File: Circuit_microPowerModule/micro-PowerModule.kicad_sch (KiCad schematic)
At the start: 7 parts, among them J2 Jack-DC, J3 Screw_Terminal_01x02

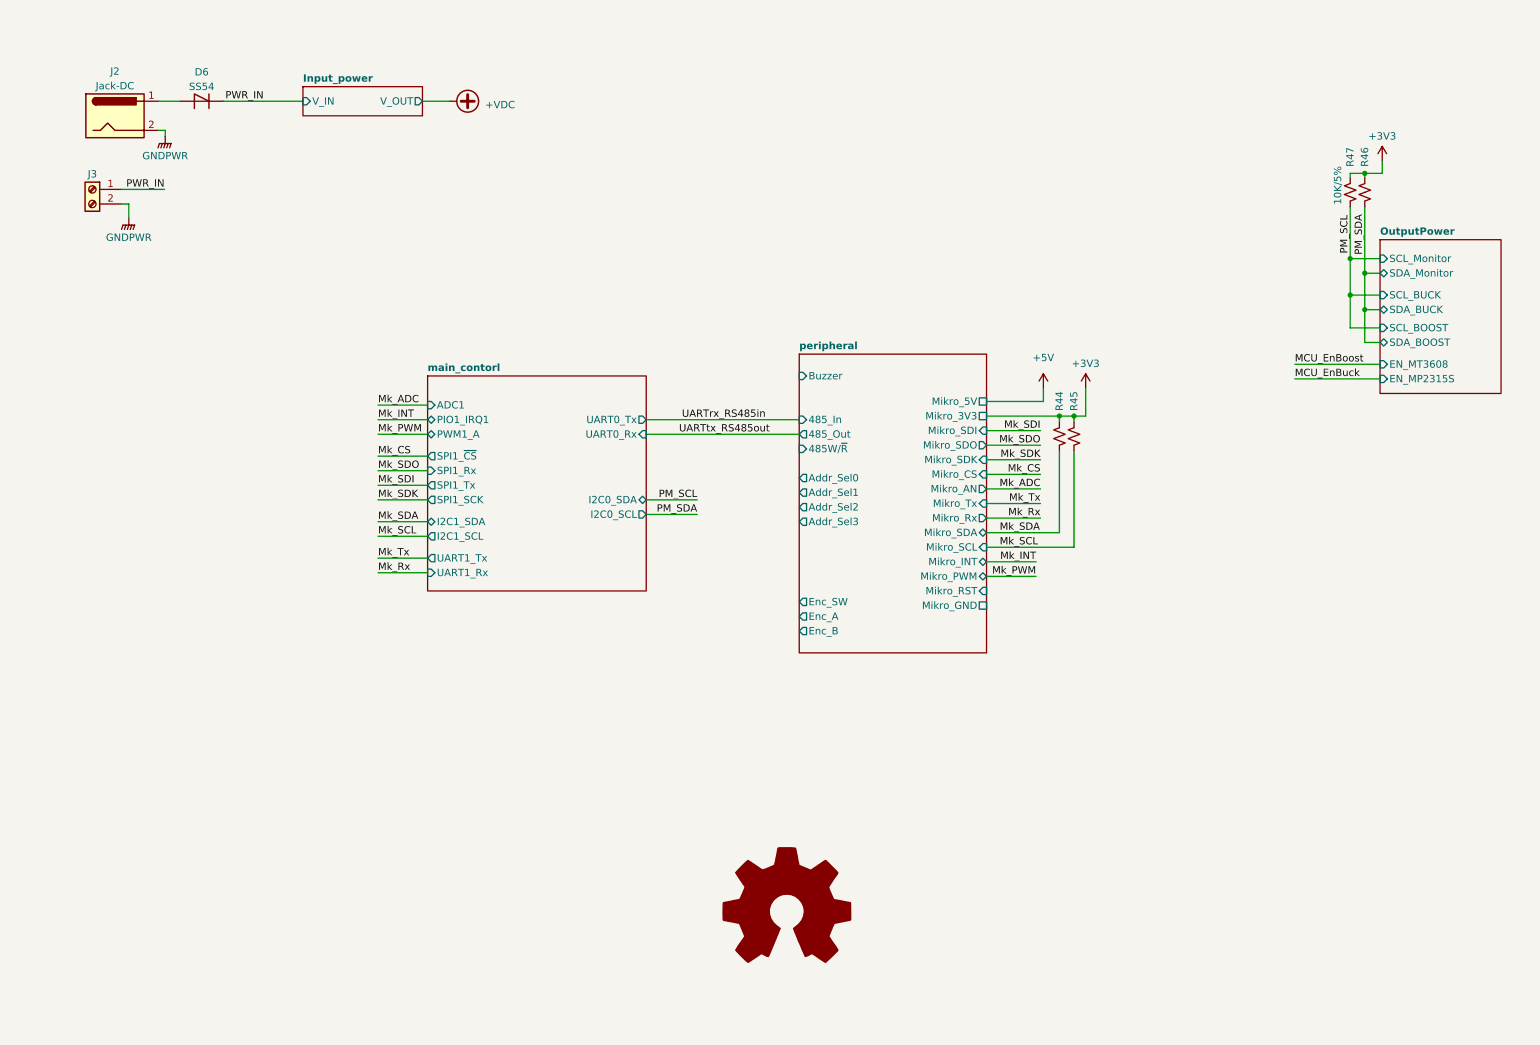
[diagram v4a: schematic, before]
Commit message: Completed microcontroller unit pin planning
update schematic
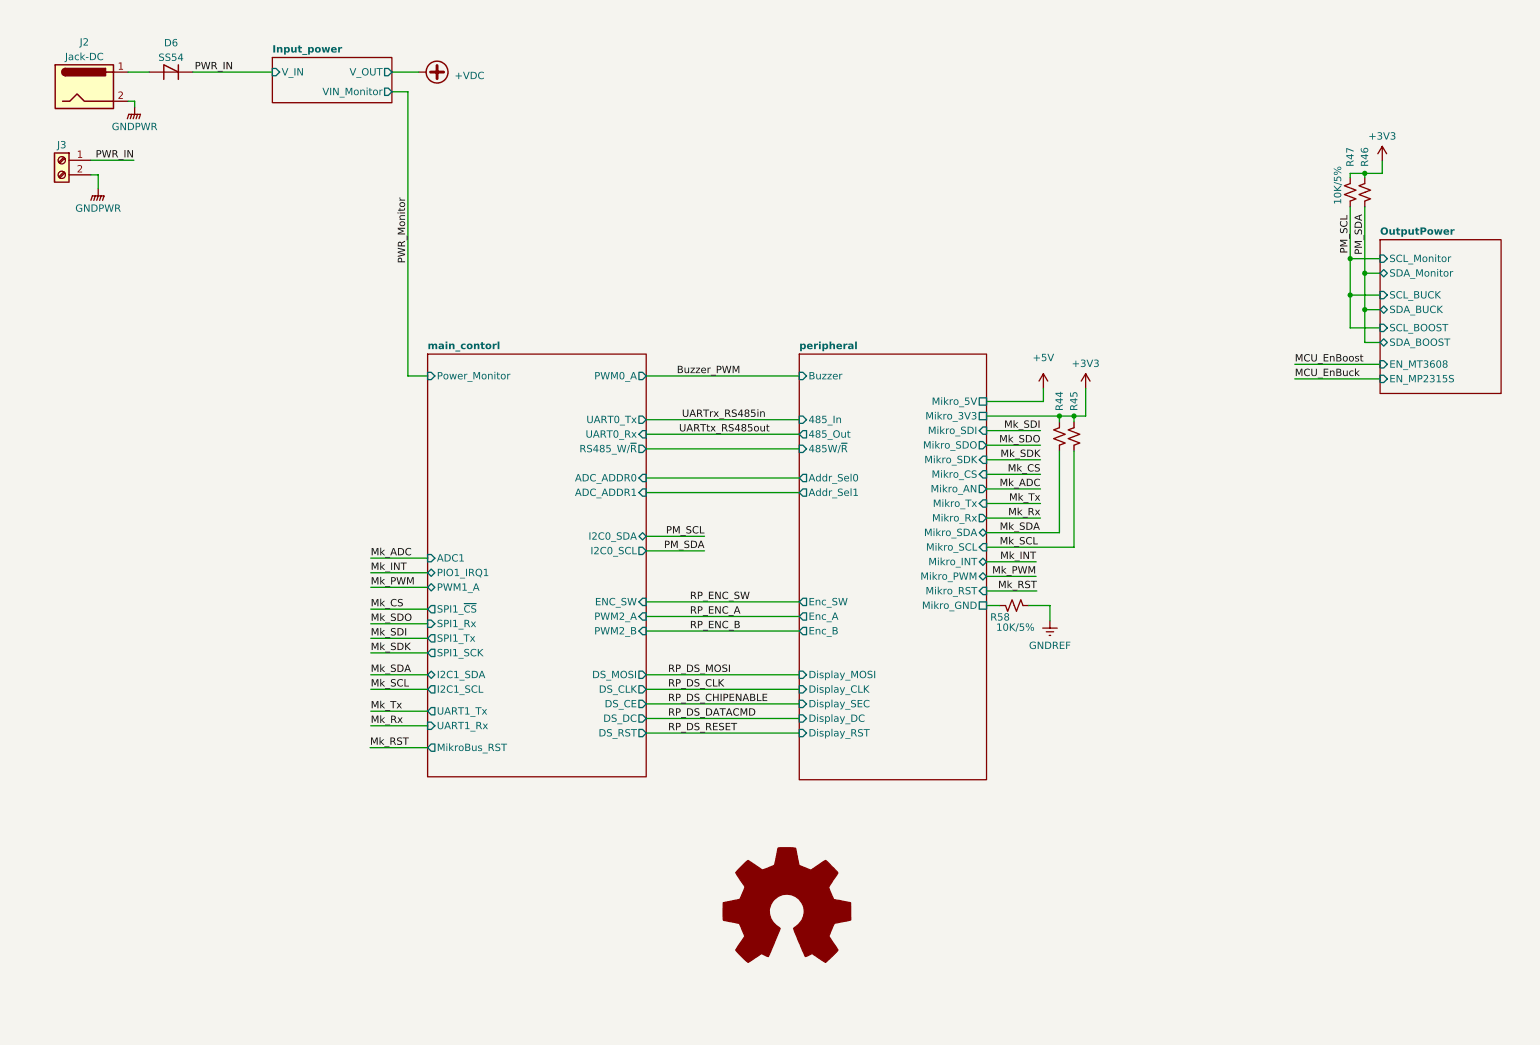
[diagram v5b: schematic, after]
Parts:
- added R58: 10K/5%, Resistor_SMD:R_0603_1608Metric, symbol Device:R_Small_US
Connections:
- net peripheral/Mikro_GND: now also R58.2
- new net GNDREF: R58.1
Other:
- sheet Input_power ports: added VIN_Monitor; removed none
- sheet main_contorl ports: added ADC_ADDR0, ADC_ADDR1, DS_CE, DS_CLK, DS_DC, DS_MOSI, DS_RST, ENC_SW, MikroBus_RST, PWM0_A, PWM2_A, PWM2_B, Power_Monitor, RS485_W/~{R}; removed none
- sheet peripheral ports: added Display_CLK, Display_DC, Display_MOSI, Display_RST, Display_SEC; removed Addr_Sel2, Addr_Sel3
- moved on the sheet: D6, J2, J3

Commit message: change licenses
updated some footprint, create nokia 5110 lcd module pcb symbol, updated reademe
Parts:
- D6: footprint (none) -> Diode_SMD:D_SMA
- J2: footprint (none) -> Connector_BarrelJack:BarrelJack_Wuerth_6941xx301002
- J3: footprint (none) -> Connector_Phoenix_MC:PhoenixContact_MC_1,5_2-G-3.81_1x02_P3.81mm_Horizontal
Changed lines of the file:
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@@
       (effects (font (size 1.27 1.27)))
     )
-    (property "Footprint" "" (at 39.243 34.417 0)
+    (property "Footprint" "Connector_BarrelJack:BarrelJack_Wuerth_6941xx301002" (at 39.243 34.417 0)
       (effects (font (size 1.27 1.27)) hide)
     )
@@
       (effects (font (size 1.27 1.27)))
     )
-    (property "Footprint" "" (at 53.086 30.861 0)
+    (property "Footprint" "Diode_SMD:D_SMA" (at 53.086 30.861 0)
       (effects (font (size 1.27 1.27)) hide)
     )
@@
       (effects (font (size 1.27 1.27)) hide)
     )
-    (property "Footprint" "" (at 34.036 46.228 0)
-      (effects (font (size 1.27 1.27)) hide)
-    )
+    (property "Footprint" "Connector_Phoenix_MC:PhoenixContact_MC_1,5_2-G-3.81_1x02_P3.81mm_Horizontal" (at 34.036 46.228 0)
+      (effects (font (size 1.27 1.27)) hide)
+    )

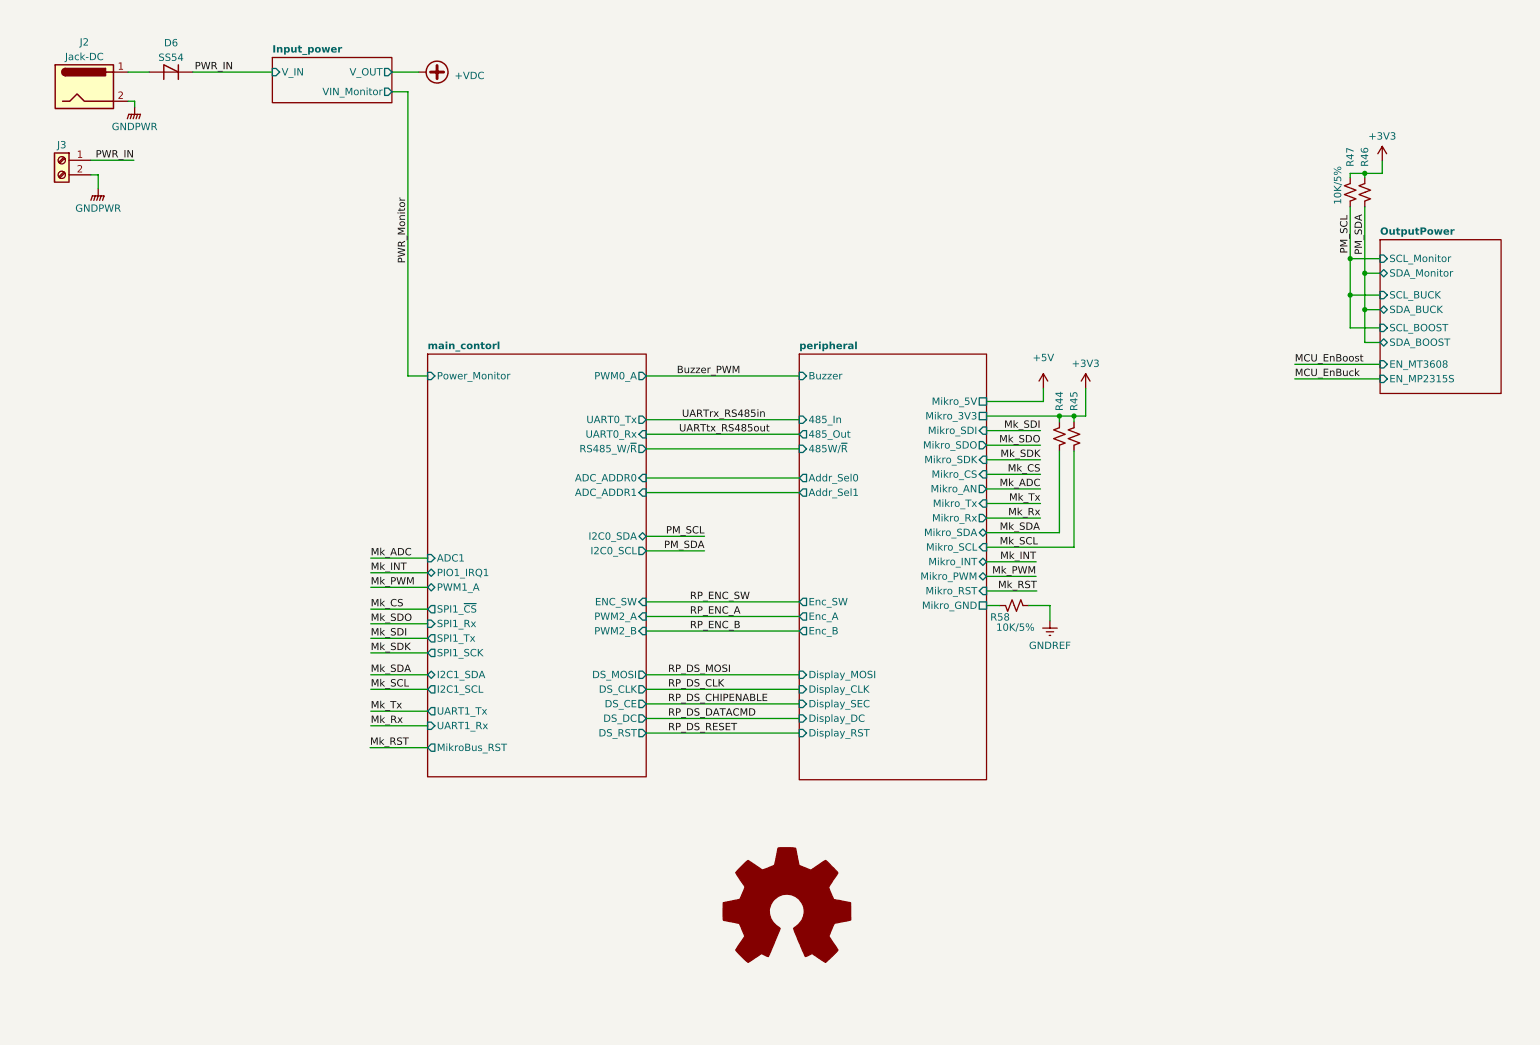
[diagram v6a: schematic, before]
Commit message: update schematic
added pin assessment to readme
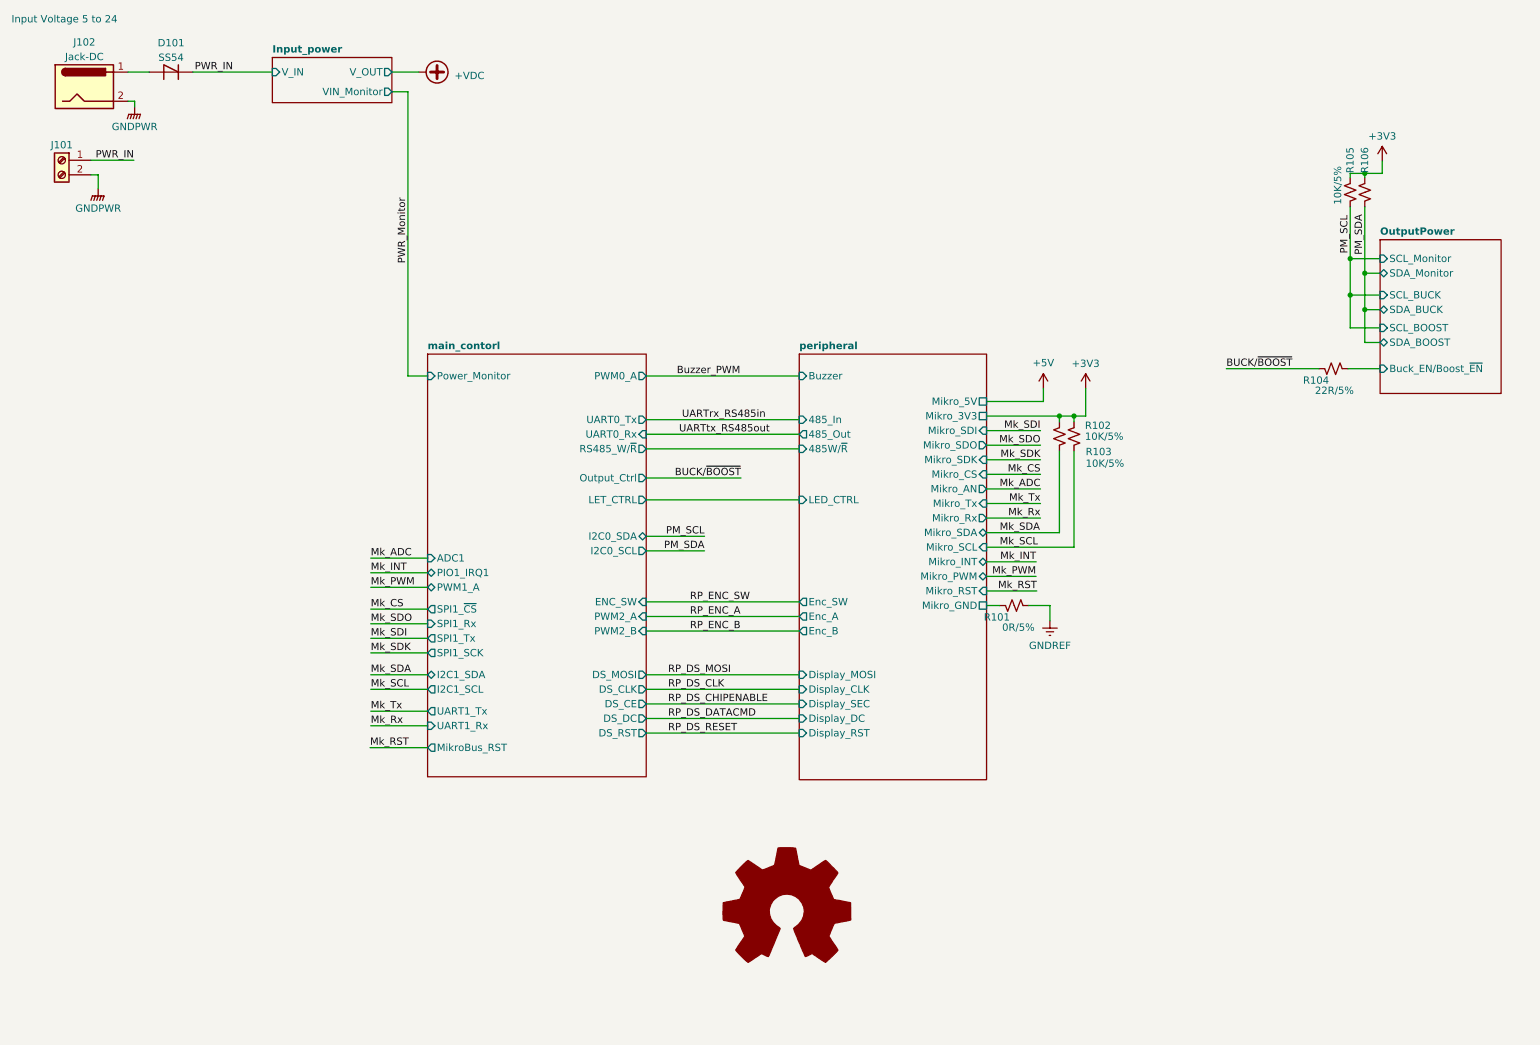
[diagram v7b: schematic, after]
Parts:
- added R104: 22R/5%, Resistor_SMD:R_0603_1608Metric, symbol Device:R_Small_US
- R101: renamed from R58; value 10K/5% -> 0R/5%
- renumbered D6 to D101, J3 to J101, J2 to J102, R44 to R102, R45 to R103, R47 to R105, R46 to R106
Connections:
- new net BUCK/~{BOOST}: R104.2
- new net OutputPower/Buck_EN/Boost_~{EN}: R104.1
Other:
- sheet OutputPower ports: added Buck_EN/Boost_~{EN}; removed EN_MP2315S, EN_MT3608
- sheet main_contorl ports: added LET_CTRL, Output_Ctrl; removed ADC_ADDR0, ADC_ADDR1
- sheet peripheral ports: added LED_CTRL; removed Addr_Sel0, Addr_Sel1
- note added: "Input Voltage 5 to 24"
